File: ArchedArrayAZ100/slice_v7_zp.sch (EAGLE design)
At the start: 118 parts

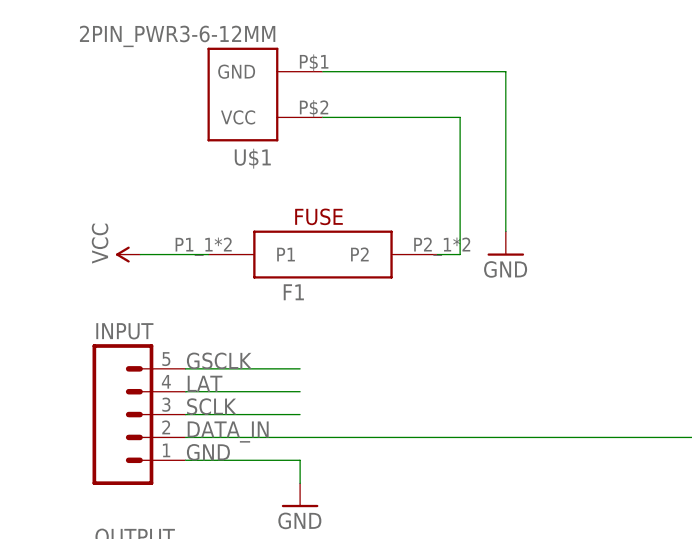
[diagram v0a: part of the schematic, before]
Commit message: added slice_v7 ArchedArray with 4 layers
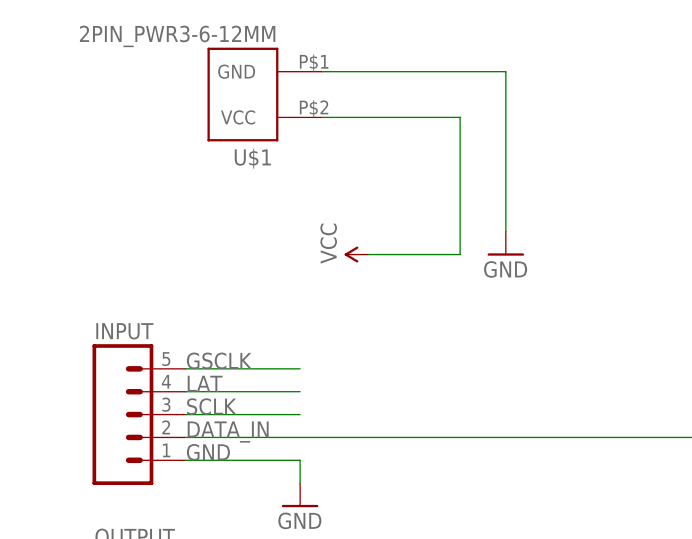
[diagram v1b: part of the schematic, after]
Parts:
- removed F1: (no value), ZacksLib2:FUSE_2PIN0
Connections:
- removed net N$284: F1.P2, U$1.VCC
- net VCC: now also U$1.VCC; no longer F1.P1
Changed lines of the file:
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@@
 <part name="GND6" library="SparkFun-Aesthetics" deviceset="GND" device=""/>
 <part name="GND7" library="SparkFun-Aesthetics" deviceset="GND" device=""/>
-<part name="F1" library="ZacksLib2" deviceset="FUSE_2PIN" device="0" value=" "/>
 <part name="GND8" library="SparkFun-Aesthetics" deviceset="GND" device=""/>
 <part name="GND9" library="SparkFun-Aesthetics" deviceset="GND" device=""/>
@@
 <instance part="D96" gate="G$1" x="147.32" y="-269.24" rot="R270"/>
 <instance part="SUPPLY6" gate="G$1" x="124.46" y="-215.9"/>
-<instance part="SUPPLY7" gate="G$1" x="-213.36" y="215.9" rot="R90"/>
+<instance part="SUPPLY7" gate="G$1" x="-187.96" y="215.9" rot="R90"/>
 <instance part="C1" gate="G$1" x="-27.94" y="22.86" rot="R90"/>
 <instance part="C2" gate="G$1" x="269.24" y="-139.7" rot="R90"/>
@@
 <instance part="GND6" gate="1" x="254" y="-195.58" rot="R90"/>
 <instance part="GND7" gate="1" x="-43.18" y="-22.86" rot="R90"/>
-<instance part="F1" gate="G$1" x="-193.04" y="215.9"/>
 <instance part="GND8" gate="1" x="-195.58" y="187.96"/>
 <instance part="GND9" gate="1" x="-195.58" y="165.1"/>
@@
 </segment>
 <segment>
+<wire x1="-193.04" y1="231.14" x2="-177.8" y2="231.14" width="0.1524" layer="91"/>
+<wire x1="-177.8" y1="215.9" x2="-177.8" y2="231.14" width="0.1524" layer="91"/>
+<pinref part="U$1" gate="G$1" pin="VCC"/>
 <pinref part="SUPPLY7" gate="G$1" pin="VCC"/>
-<pinref part="F1" gate="G$1" pin="P1"/>
-<wire x1="-213.36" y1="215.9" x2="-205.74" y2="215.9" width="0.1524" layer="91"/>
+<wire x1="-177.8" y1="215.9" x2="-187.96" y2="215.9" width="0.1524" layer="91"/>
 </segment>
 </net>
@@
 </segment>
 </net>
-<net name="N$284" class="0">
-<segment>
-<wire x1="-193.04" y1="231.14" x2="-177.8" y2="231.14" width="0.1524" layer="91"/>
-<pinref part="F1" gate="G$1" pin="P2"/>
-<wire x1="-180.34" y1="215.9" x2="-177.8" y2="215.9" width="0.1524" layer="91"/>
-<wire x1="-177.8" y1="215.9" x2="-177.8" y2="231.14" width="0.1524" layer="91"/>
-<pinref part="U$1" gate="G$1" pin="VCC"/>
-</segment>
-</net>

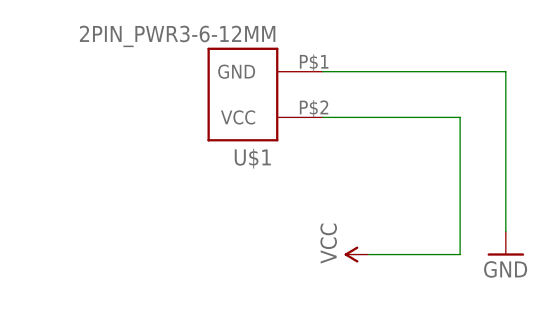
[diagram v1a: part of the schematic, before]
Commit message: added changes to ArchedArray board according to email
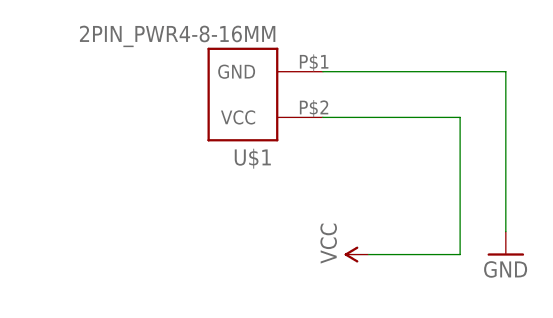
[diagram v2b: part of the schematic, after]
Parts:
- U$1: value 2PIN_PWR3-6-12MM -> 2PIN_PWR4-8-16MM; device WallerLabLib:2PIN_PWR3-6-12MM -> WallerLabLib:2PIN_PWR4-8-16MM
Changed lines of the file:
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@@
 <layer number="112" name="tSilk" color="7" fill="1" visible="yes" active="yes"/>
 <layer number="113" name="IDFDebug" color="4" fill="1" visible="no" active="yes"/>
+<layer number="114" name="Badge_Outline" color="7" fill="1" visible="yes" active="yes"/>
+<layer number="115" name="ReferenceISLANDS" color="7" fill="1" visible="yes" active="yes"/>
 <layer number="116" name="Patch_BOT" color="9" fill="4" visible="no" active="yes"/>
 <layer number="118" name="Rect_Pads" color="7" fill="1" visible="yes" active="yes"/>
@@
 <part name="GND14" library="SparkFun-Aesthetics" deviceset="GND" device=""/>
 <part name="GND15" library="SparkFun-Aesthetics" deviceset="GND" device=""/>
-<part name="U$1" library="WallerLabLib" deviceset="2PIN_PWR" device="3-6-12MM"/>
+<part name="U$1" library="WallerLabLib" deviceset="2PIN_PWR" device="4-8-16MM" value="2PIN_PWR4-8-16MM"/>
 </parts>
 <sheets>
